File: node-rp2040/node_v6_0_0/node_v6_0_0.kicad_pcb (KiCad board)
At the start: 6 copper layers, 45 x 75 mm, 91 parts, among them J1 PJ-014D, J10 Connector, USB-TYPE-C-16P, J11 Conn_01x08, J12 Conn_01x08, J2 U.FL, J3 Conn_Coaxial, J6 U.FL, J7 Conn_01x02_Pin, J8 PJ-014D, J9 U.FL, Q1 DMG2301L, SW2 PTS636 SM50J SMTR LFS, SW3 PTS636 SM50J SMTR LFS, U1 RP2040, U11 1042240820, U12 CAT24M01W, U14 W25Q128, U2 USBLC6-2SC6, U3 AP2112K-3.3, U5 MCP73831-2-OT, U6 RFM69HCW, U7 PCF8523T, U8 SP3485EN, U9 SIM7080G

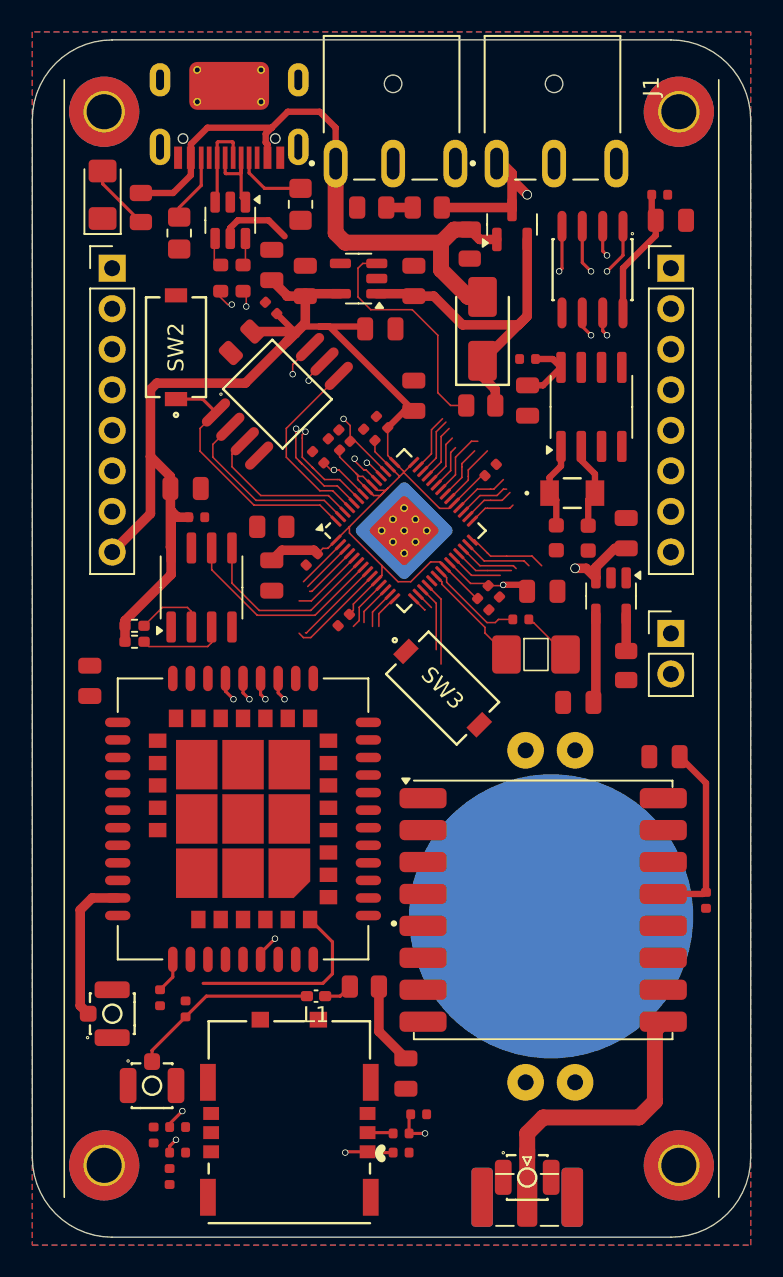
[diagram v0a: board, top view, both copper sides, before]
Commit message: finished initial routing
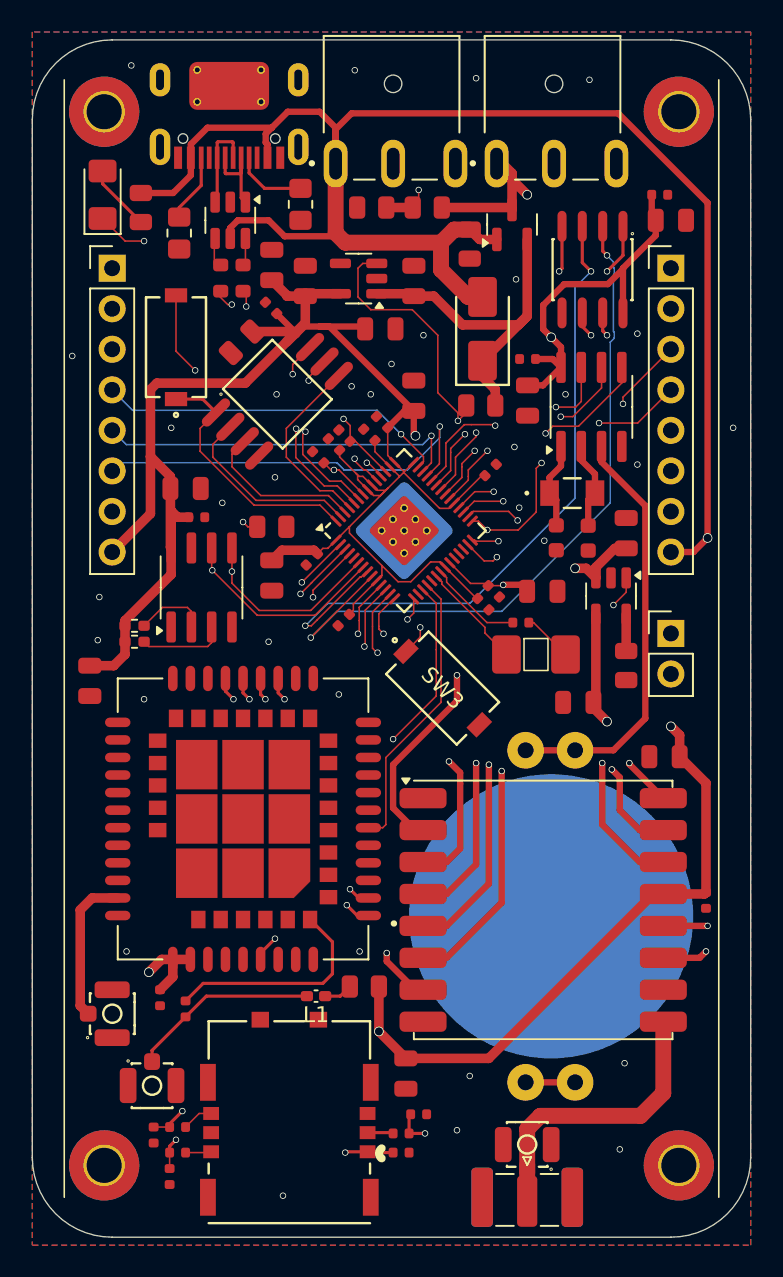
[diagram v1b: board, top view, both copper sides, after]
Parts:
- added G***: LOGO, WiSDOM:wisdomcat, B.Cu at (151.8, 89.0)
- added G***: LOGO, logos:wisdom_logo_lineborder, B.Cu at (152.2, 108.3)
- added LOGO: , logos:github_qr, B.Cu at (146.7, 134.1)
- added LOGO: , logos:qrcode, B.Cu at (146.7, 120.2)
- moved J2 0.55 mm to (161.0, 139.4), turned to 90 degrees
- moved R5 0.20 mm to (160.6, 106.0)
- turned C35 to -90 degrees
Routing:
- net +3.3V: track 144.4 -> 237.7 mm, vias 0 -> 5
- net VBUS: track 50.8 -> 124.0 mm, vias 0 -> 2
- net Net-(D1-K): track 0.00 -> 56.4 mm, vias 0 -> 5
- net SCL: track 13.3 -> 67.7 mm, vias 0 -> 2
- net SDA: track 12.1 -> 65.6 mm, vias 0 -> 2
- net Net-(BT1-+): track 0.00 -> 50.4 mm
- net TX1: track 6.19 -> 48.5 mm, vias 1 -> 4
- net SPI_CK: track 3.02 -> 44.9 mm, vias 0 -> 4
- net RX1: track 5.85 -> 47.3 mm, vias 1 -> 3
- net RFM_DIO3: track 3.47 -> 43.7 mm, vias 0 -> 2
- net RFM_DIO4: track 4.22 -> 44.2 mm, vias 0 -> 2
- net MOSI: track 3.26 -> 42.8 mm, vias 0 -> 2
- net RFM_DIO5: track 2.84 -> 42.0 mm, vias 0 -> 2
- net 485_!RE: track 8.22 -> 45.5 mm, vias 1 -> 2
- net MISO: track 4.37 -> 39.6 mm, vias 0 -> 3
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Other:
- board text added: "WiSDOM GitHub"
- board text added: "WiSDOM Node v6.0.0 Design by Amelia Vlahogiannis May 2025"
- board text added: "wisdomresearch.net"

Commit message: added silkscreens, fixed missing caps on RP2040 XTAL
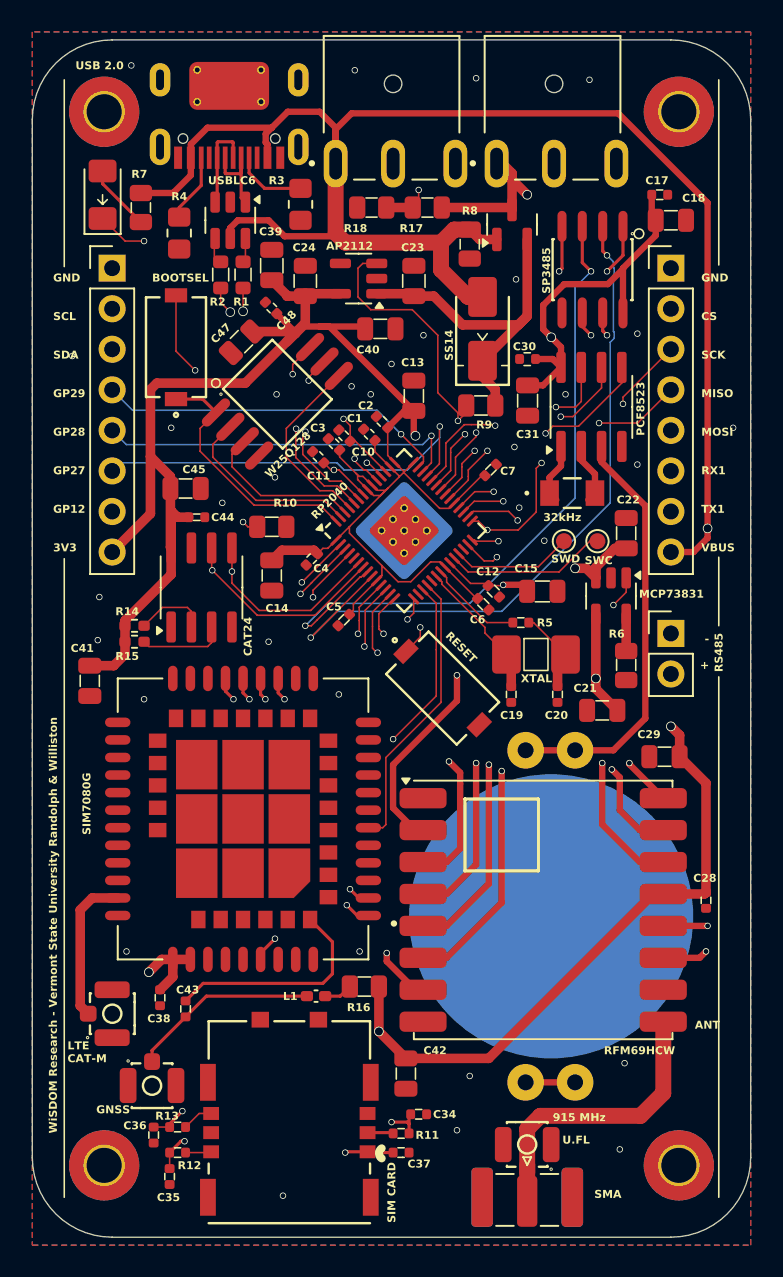
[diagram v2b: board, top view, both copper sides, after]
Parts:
- removed C32, C33: 6p, JLCPCB:C_0603
- added C19: 15p, JLCPCB:C_0402, F.Cu at (160.0, 110.5)
- added C20: 15p, JLCPCB:C_0402, F.Cu at (162.9, 110.5)
- added REF**: TestPoint_Pad_D1.0mm, TestPoint:TestPoint_Pad_D1.0mm, F.Cu at (165.4, 100.9)
- added REF**: TestPoint_Pad_D1.0mm, TestPoint:TestPoint_Pad_D1.0mm, F.Cu at (163.3, 100.9)
- added REF**: KiCad-Logo2_5mm_SilkScreen, Symbol:KiCad-Logo2_5mm_SilkScreen, B.Cu at (161.4, 108.7)
- added REF**: OSHW-Logo_5.7x6mm_SilkScreen, Symbol:OSHW-Logo_5.7x6mm_SilkScreen, B.Cu at (156.5, 101.4)
- moved G*** 16.6 mm to (152.3, 91.7)
- moved G*** 12.6 mm to (145.7, 100.0)
- moved C21 1.58 mm to (165.7, 111.5)
- moved R1 0.20 mm to (143.2, 84.2)
- moved R2 0.20 mm to (141.8, 84.2)
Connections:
- J2 pad 3: GND -> (no net)
- J6 pad 3: GND -> (no net)
- J9 pad 3: GND -> (no net)
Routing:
- net SWCLK: track 0.00 -> 10.1 mm
- net SWD: track 0.00 -> 7.58 mm
- net /PERIPHERALS/SIM_RST: track 38.3 -> 36.0 mm
- net Net-(C20-Pad1): track 2.93 -> 5.14 mm
- net /MCU/XTAL+: track 6.79 -> 8.92 mm
- net /PERIPHERALS/RTC_X2: track 5.50 -> 3.88 mm
- net /PERIPHERALS/RTC_X1: track 5.42 -> 3.82 mm
- net VBUS: track 124.0 -> 125.0 mm
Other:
- board text added: "+ -"
- board text added: "32kHz"
- board text added: "915 MHz"
- board text added: "ANT"
- board text added: "AP2112"
- board text added: "BAT"
- board text added: "BOOTSEL"
- board text added: "C1"
- board text added: "C10"
- board text added: "C11"
- board text added: "C12"
- board text added: "C13"
- board text added: "C14"
- board text added: "C15"
- board text added: "C17"
- board text added: "C18"
- board text added: "C19"
- board text added: "C2"
- board text added: "C20"
- board text added: "C21"
- board text added: "C22"
- board text added: "C23"
- board text added: "C24"
- board text added: "C28"
- board text added: "C29"
- board text added: "C3"
- board text added: "C30"
- board text added: "C31"
- board text added: "C34"
- board text added: "C35"
- board text added: "C36"
- board text added: "C37"
- board text added: "C38"
- board text added: "C39"
- board text added: "C4"
- board text added: "C40"
- board text added: "C41"
- board text added: "C42"
- board text added: "C43"
- board text added: "C44"
- board text added: "C45"
- board text added: "C47"
- board text added: "C48"
- board text added: "C5"
- board text added: "C6"
- board text added: "C7"
- board text added: "CAT24"
- board text added: "GND CS SCK MISO MOSI RX1 TX1 VBUS"
- board text added: "GND SCL SDA GP29 GP28 GP27 GP12 3V3"
- board text added: "GNSS"
- board text added: "L1"
- board text added: "LTE CAT-M"
- board text added: "MCP73831"
- board text added: "PCF8523"
- board text added: "R10"
- board text added: "R11"
- board text added: "R12"
- board text added: "R13"
- board text added: "R14"
- board text added: "R15"
- board text added: "R16"
- board text added: "R17"
- board text added: "R18"
- board text added: "R2 R1"
- board text added: "R3"
- board text added: "R4"
- board text added: "R5"
- board text added: "R6"
- board text added: "R7"
- board text added: "R8"
- board text added: "R9"
- board text added: "RESET"
- board text added: "RFM69HCW"
- board text added: "RP2040"
- board text added: "RS485"
- board text added: "SIM CARD"
- board text added: "SIM7080G"
- board text added: "SMA"
- board text added: "SP3485"
- board text added: "SS14"
- board text added: "SWC"
- board text added: "SWD"
- board text added: "U.FL"
- board text added: "USB 2.0"
- board text added: "USBLC6"
- board text added: "VBUS"
- board text added: "W25Q128"
- board text added: "WiSDOM Research - Vermont State University Randolph & Williston"
- board text added: "XTAL"

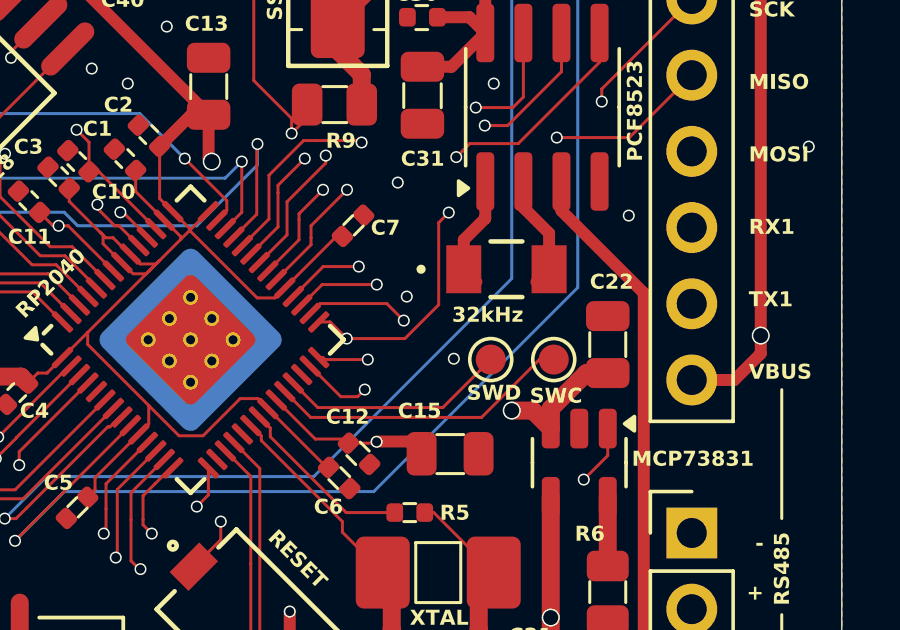
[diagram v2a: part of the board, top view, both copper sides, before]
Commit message: moved SWD pads, confirmed DRC ok
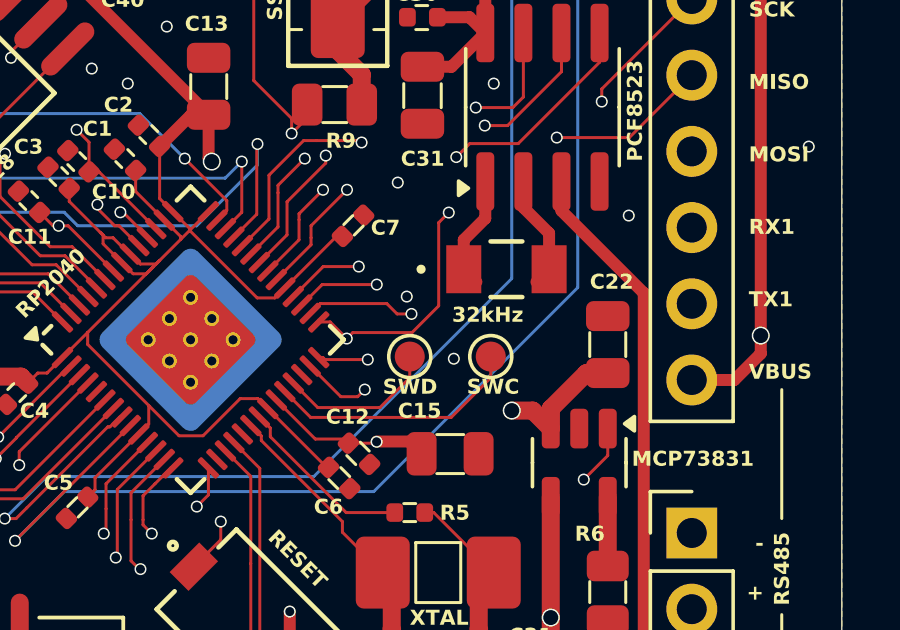
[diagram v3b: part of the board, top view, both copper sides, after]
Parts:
- moved REF** 2.70 mm to (160.6, 100.8)
- moved REF** 2.10 mm to (163.3, 100.8)
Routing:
- net SWD: track 7.58 -> 5.34 mm
- net SWCLK: track 10.1 -> 8.48 mm
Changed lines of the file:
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@@
 	(footprint "TestPoint:TestPoint_Pad_D1.0mm"
 		(layer "F.Cu")
-		(at 165.4 100.9)
+		(at 163.3 100.8)
 		(descr "SMD pad as test Point, diameter 1.0mm")
 		(tags "test point SMD pad")
@@
 	(footprint "TestPoint:TestPoint_Pad_D1.0mm"
 		(layer "F.Cu")
-		(at 163.3 100.9)
+		(at 160.6 100.8)
 		(descr "SMD pad as test Point, diameter 1.0mm")
 		(tags "test point SMD pad")
@@
 	)
 	(gr_text "SWC"
-		(at 164.6 102.4 0)
+		(at 162.5 102.1 0)
 		(layer "F.SilkS")
 		(effects
@@
 	)
 	(gr_text "SWD"
-		(at 162.5 102.3 0)
+		(at 159.7 102.1 0)
 		(layer "F.SilkS")
 		(effects
@@
 	)
 	(segment
+		(start 157.613107 99.033268)
+		(end 157.282842 99.363533)
+		(width 0.1)
+		(layer "F.Cu")
+		(net 24)
+	)
+	(segment
 		(start 156.8 120.15)
 		(end 156.8 116.1)
@@
 	)
 	(segment
-		(start 157.613107 99.033268)
-		(end 159.833268 99.033268)
+		(start 160.657871 99.378861)
+		(end 160.178861 99.378861)
 		(width 0.1)
 		(layer "F.Cu")
@@
 	)
 	(segment
-		(start 159.833268 99.033268)
-		(end 160.4 99.6)
-		(width 0.1)
+		(start 156.8 116.1)
+		(end 156.8 115.4)
+		(width 0.4)
 		(layer "F.Cu")
 		(net 24)
 	)
 	(segment
-		(start 156.8 116.1)
-		(end 156.8 115.4)
+		(start 154.475 121)
+		(end 155.95 121)
 		(width 0.4)
 		(layer "F.Cu")
@@
 	)
 	(segment
-		(start 157.282842 99.363533)
+		(start 159.833268 99.033268)
 		(end 157.613107 99.033268)
 		(width 0.1)
@@
 	)
 	(segment
-		(start 154.475 121)
-		(end 155.95 121)
+		(start 156.8 115.4)
+		(end 156.1 114.7)
 		(width 0.4)
 		(layer "F.Cu")
@@
 	)
 	(segment
-		(start 156.8 115.4)
-		(end 156.1 114.7)
-		(width 0.4)
+		(start 160.178861 99.378861)
+		(end 159.833268 99.033268)
+		(width 0.1)
 		(layer "F.Cu")
 		(net 24)
@@
 	)
 	(via
-		(at 160.4 99.6)
+		(at 160.657871 99.378861)
 		(size 0.4)
 		(drill 0.3)
@@
 	)
 	(segment
-		(start 160.4 99.6)
-		(end 159.862189 99.6)
+		(start 159.862189 99.6)
+		(end 156.1 103.362189)
 		(width 0.1)
 		(layer "In2.Cu")
@@
 	)
 	(segment
-		(start 159.862189 99.6)
-		(end 156.1 103.362189)
+		(start 160.657871 99.378861)
+		(end 160.436732 99.6)
 		(width 0.1)
 		(layer "In2.Cu")
@@
 	)
 	(segment
-		(start 170 93.96)
-		(end 169.04 93)
+		(start 160.436732 99.6)
+		(end 159.862189 99.6)
+		(width 0.1)
+		(layer "In2.Cu")
+		(net 24)
+	)
+	(segment
+		(start 169.04 93)
+		(end 170 93.96)
 		(width 0.1)
 		(layer "In4.Cu")
@@
 	)
 	(segment
-		(start 162.351 95.974678)
-		(end 162.351 97.649)
+		(start 160.657871 99.378861)
+		(end 160.657871 99.342129)
 		(width 0.1)
 		(layer "In4.Cu")
@@
 	)
 	(segment
-		(start 169.04 93)
-		(end 165.325678 93)
+		(start 162.351 97.649)
+		(end 162.351 95.974678)
 		(width 0.1)
 		(layer "In4.Cu")
@@
 	(segment
 		(start 165.325678 93)
-		(end 162.351 95.974678)
+		(end 169.04 93)
 		(width 0.1)
 		(layer "In4.Cu")
@@
 	)
 	(segment
-		(start 162.351 97.649)
-		(end 160.4 99.6)
+		(start 160.657871 99.342129)
+		(end 162.351 97.649)
+		(width 0.1)
+		(layer "In4.Cu")
+		(net 24)
+	)
+	(segment
+		(start 162.351 95.974678)
+		(end 165.325678 93)
 		(width 0.1)
 		(layer "In4.Cu")
@@
 	)
 	(segment
+		(start 160.674543 100)
+		(end 158.7 100)
+		(width 0.1)
+		(layer "F.Cu")
+		(net 31)
+	)
+	(segment
 		(start 167 91.88)
 		(end 170 88.88)
@@
 	)
 	(segment
-		(start 160.437811 100.2)
-		(end 161.5648 99.073011)
-		(width 0.1)
-		(layer "F.Cu")
-		(net 31)
-	)
-	(segment
-		(start 161.5648 96.3352)
-		(end 161.9 96)
+		(start 161.9 96)
+		(end 161.5648 96.3352)
 		(width 0.1)
 		(layer "F.Cu")
@@
 	)
 	(segment
-		(start 161.5648 99.073011)
-		(end 161.5648 96.3352)
+		(start 158.7 100)
+		(end 158.5 100.2)
 		(width 0.1)
 		(layer "F.Cu")
@@
 	)
 	(segment
-		(start 158.5 100.2)
-		(end 160.437811 100.2)
+		(start 161.5648 99.109743)
+		(end 160.674543 100)
 		(width 0.1)
 		(layer "F.Cu")
@@
 		(net 31)
 	)
+	(segment
+		(start 161.5648 96.3352)
+		(end 161.5648 99.109743)
+		(width 0.1)
+		(layer "F.Cu")
+		(net 31)
+	)
 	(via
 		(at 158.5 100.2)
@@
 	)
 	(segment
-		(start 156.434314 101.965686)
-		(end 157.29686 102.828232)
+		(start 157.29686 102.828232)
+		(end 161.978874 102.828232)
 		(width 0.1)
 		(layer "F.Cu")
@@
 	)
 	(segment
-		(start 157.29686 102.828232)
-		(end 162.992536 102.828232)
+		(start 161.978874 102.828232)
+		(end 163.3 101.507106)
 		(width 0.1)
 		(layer "F.Cu")
@@
 	)
 	(segment
-		(start 164.920768 100.9)
-		(end 165.4 100.9)
+		(start 163.3 101.507106)
+		(end 163.3 100.8)
 		(width 0.1)
 		(layer "F.Cu")
@@
 	)
 	(segment
-		(start 162.992536 102.828232)
-		(end 164.920768 100.9)
+		(start 156.434314 101.965686)
+		(end 157.29686 102.828232)
 		(width 0.1)
 		(layer "F.Cu")
@@
 	)
 	(segment
-		(start 161.7 102.5)
-		(end 163.3 100.9)
+		(start 160.6 101.507106)
+		(end 160.6 100.8)
 		(width 0.1)
 		(layer "F.Cu")
@@
 	(segment
 		(start 157.534314 102.5)
-		(end 161.7 102.5)
+		(end 159.607106 102.5)
+		(width 0.1)
+		(layer "F.Cu")
+		(net 33)
+	)
+	(segment
+		(start 159.607106 102.5)
+		(end 160.6 101.507106)
 		(width 0.1)
 		(layer "F.Cu")
